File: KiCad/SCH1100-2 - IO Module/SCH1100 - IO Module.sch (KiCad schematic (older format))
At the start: 10 parts, among them J1 Headset In, J2 3.5mm Audio In, J3 Radio In, P1 Mates With A1A1J1, P2 Mates With A1A1J2, P3 Mates with A1A1J3, P4 Mates With A1A1J4, SW1 Power / Input Switch B, SW2 Power / Input Switch A

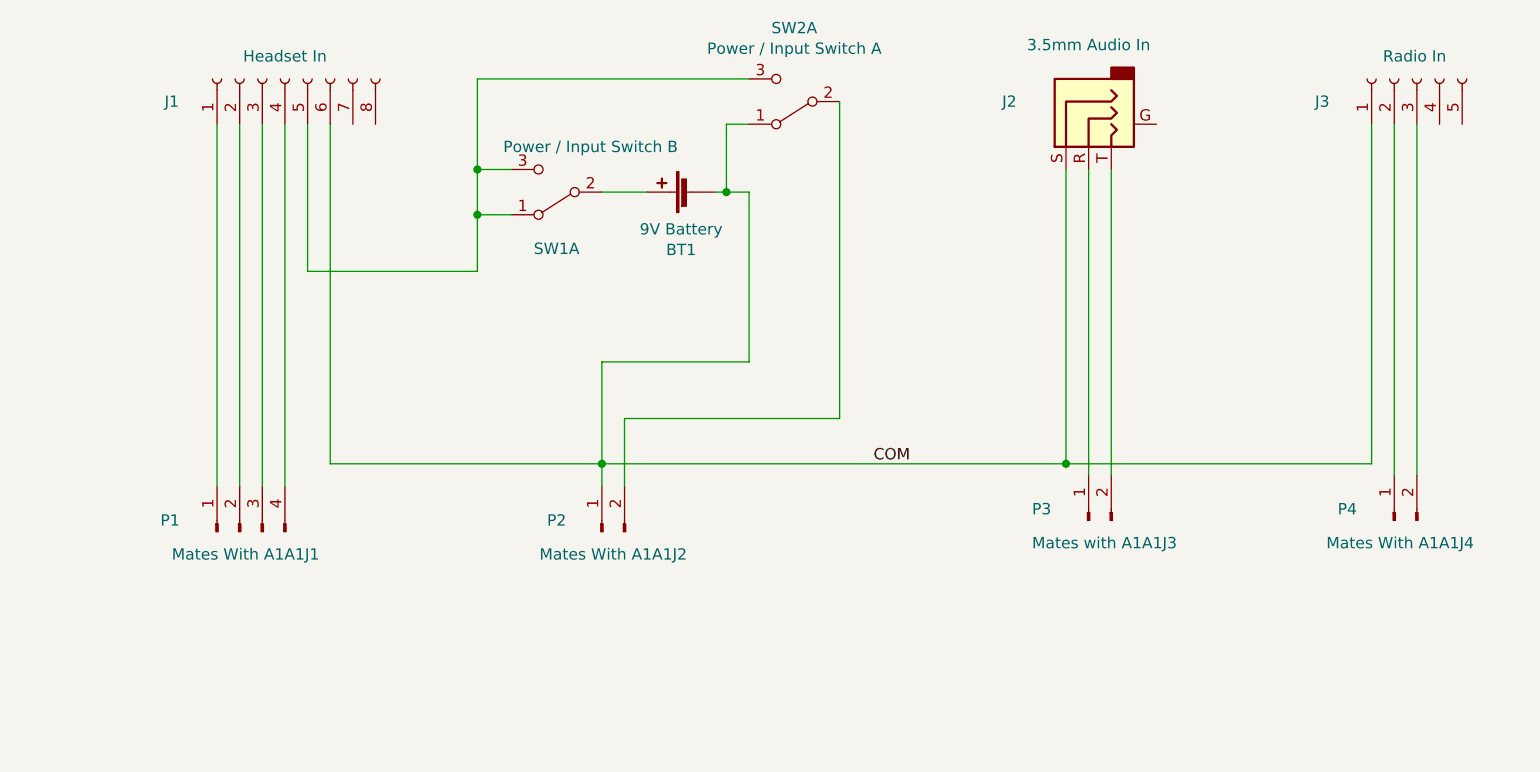
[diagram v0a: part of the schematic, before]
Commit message: Incorporated redlines for -2 PCB and wiring schematics.
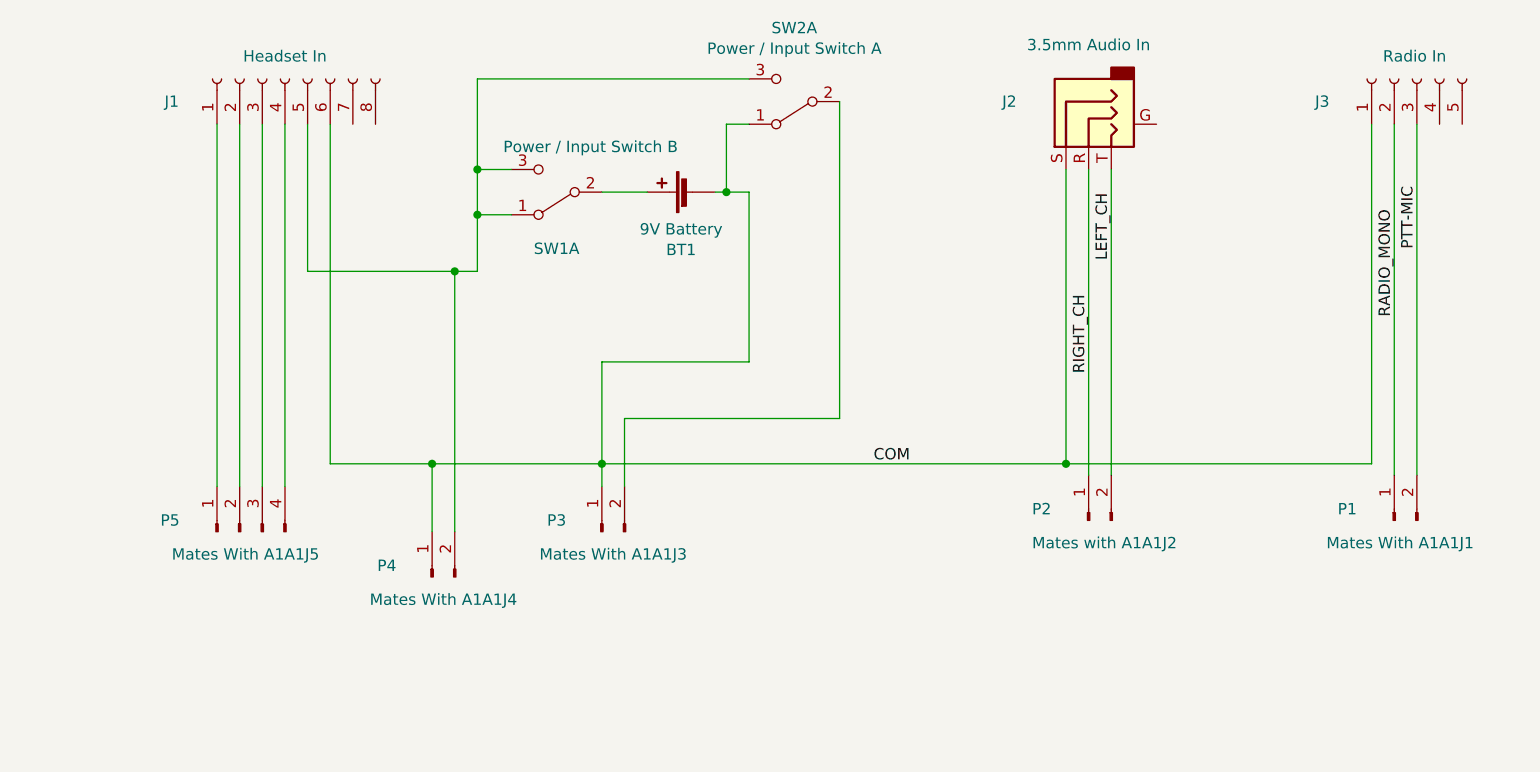
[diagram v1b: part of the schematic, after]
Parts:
- added P4: Mates With A1A1J4, symbol Connector:Conn_01x02_Male
- P1: renamed from P4; value Mates With A1A1J4 -> Mates With A1A1J1
- P2: renamed from P3; value Mates with A1A1J3 -> Mates with A1A1J2
- P3: renamed from P2; value Mates With A1A1J2 -> Mates With A1A1J3
- P5: renamed from P1; value Mates With A1A1J1 -> Mates With A1A1J5
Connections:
- net COM: now also P4.1 (Pin_1)
- net at J1.5 (Pin_5), SW1.1 (A), SW1.3 (C)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: now also P4.2 (Pin_2)
- net RIGHT_CH: now reaches J2.R, P2.1 (Pin_1)
- net LEFT_CH: now reaches J2.T, P2.2 (Pin_2)
- net RADIO_MONO: now reaches J3.2 (Pin_2), P1.1 (Pin_1)
- net PTT-MIC: now reaches J3.3 (Pin_3), P1.2 (Pin_2)
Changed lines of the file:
@@
 EESchema Schematic File Version 4
 LIBS:SCH1100 - IO Module-cache
-EELAYER 26 0
+EELAYER 29 0
 EELAYER END
 $Descr A4 11693 8268
@@
 Sheet 1 1
 Title "Wiring Schematic, IO Module"
-Date ""
-Rev "A"
-Comp "SCH1100"
+Date "2019-06-01"
+Rev "-"
+Comp "SCH1100-2"
 Comment1 "Author: Seth Tucker"
 Comment2 ""
@@
 	3350 1400 3350 2050
 Wire Wire Line
-	3350 2050 4100 2050
+	3350 2050 4000 2050
 Wire Wire Line
 	3450 1400 3450 2900
 Wire Wire Line
-	3450 2900 4650 2900
+	3450 2900 3900 2900
 Connection ~ 4650 2900
 Wire Wire Line
@@
 COM
 $Comp
-L Connector:Conn_01x04_Male P1
+L Connector:Conn_01x04_Male P5
 U 1 1 5C671BD2
 P 3050 3200
-F 0 "P1" V 3100 3550 50  0000 R CNN
-F 1 "Mates With A1A1J1" V 2950 3500 50  0000 R CNN
+F 0 "P5" V 3100 3550 50  0000 R CNN
+F 1 "Mates With A1A1J5" V 2950 3500 50  0000 R CNN
 F 2 "" H 3050 3200 50  0001 C CNN
 F 3 "~" H 3050 3200 50  0001 C CNN
@@
 $EndComp
 $Comp
-L Connector:Conn_01x02_Male P2
+L Connector:Conn_01x02_Male P3
 U 1 1 5C671C6B
 P 4650 3200
-F 0 "P2" V 4700 3400 50  0000 C CNN
-F 1 "Mates With A1A1J2" V 4550 3150 50  0000 C CNN
+F 0 "P3" V 4700 3400 50  0000 C CNN
+F 1 "Mates With A1A1J3" V 4550 3150 50  0000 C CNN
 F 2 "" H 4650 3200 50  0001 C CNN
 F 3 "~" H 4650 3200 50  0001 C CNN
@@
 $EndComp
 $Comp
-L Connector:Conn_01x02_Male P4
+L Connector:Conn_01x02_Male P1
 U 1 1 5C671CC9
 P 8150 3150
-F 0 "P4" V 8200 3400 50  0000 R CNN
-F 1 "Mates With A1A1J4" V 8050 3450 50  0000 R CNN
+F 0 "P1" V 8200 3400 50  0000 R CNN
+F 1 "Mates With A1A1J1" V 8050 3450 50  0000 R CNN
 F 2 "" H 8150 3150 50  0001 C CNN
 F 3 "~" H 8150 3150 50  0001 C CNN
@@
 $EndComp
 $Comp
-L Connector:Conn_01x02_Male P3
+L Connector:Conn_01x02_Male P2
 U 1 1 5C671D27
 P 6800 3150
-F 0 "P3" V 6850 3400 50  0000 R CNN
-F 1 "Mates with A1A1J3" V 6700 3400 50  0000 R CNN
+F 0 "P2" V 6850 3400 50  0000 R CNN
+F 1 "Mates with A1A1J2" V 6700 3400 50  0000 R CNN
 F 2 "" H 6800 3150 50  0001 C CNN
 F 3 "~" H 6800 3150 50  0001 C CNN
@@
 Text Notes 600  7650 0    50   ~ 0
 A1
+Text Label 8250 1950 1    50   ~ 0
+PTT-MIC
+Text Label 8150 2250 1    50   ~ 0
+RADIO_MONO
+Text Label 6900 2000 1    50   ~ 0
+LEFT_CH
+Text Label 6800 2500 1    50   ~ 0
+RIGHT_CH
+$Comp
+L Connector:Conn_01x02_Male P4
+U 1 1 5CF31A7E
+P 3900 3400
+F 0 "P4" V 3950 3600 50  0000 C CNN
+F 1 "Mates With A1A1J4" V 3800 3350 50  0000 C CNN
+F 2 "" H 3900 3400 50  0001 C CNN
+F 3 "~" H 3900 3400 50  0001 C CNN
+	1    3900 3400
+	0    -1   -1   0
+$EndComp
+Wire Wire Line
+	3900 3200 3900 2900
+Connection ~ 3900 2900
+Wire Wire Line
+	3900 2900 4650 2900
+Wire Wire Line
+	4000 3200 4000 2050
+Connection ~ 4000 2050
+Wire Wire Line
+	4000 2050 4100 2050
 $EndSCHEMATC
